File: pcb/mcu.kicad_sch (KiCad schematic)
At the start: 28 parts, among them J1 CON_SAMTEC_14P_2R_1m27_P_KEY_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, U3 IC_MCU_STM32F100C4T6B_48LQFP, X1 XTAL_8M_20PPM_18pF_ECS-80-18-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, X2 XTAL_32K768_10PPM_7pF_ECS-.32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

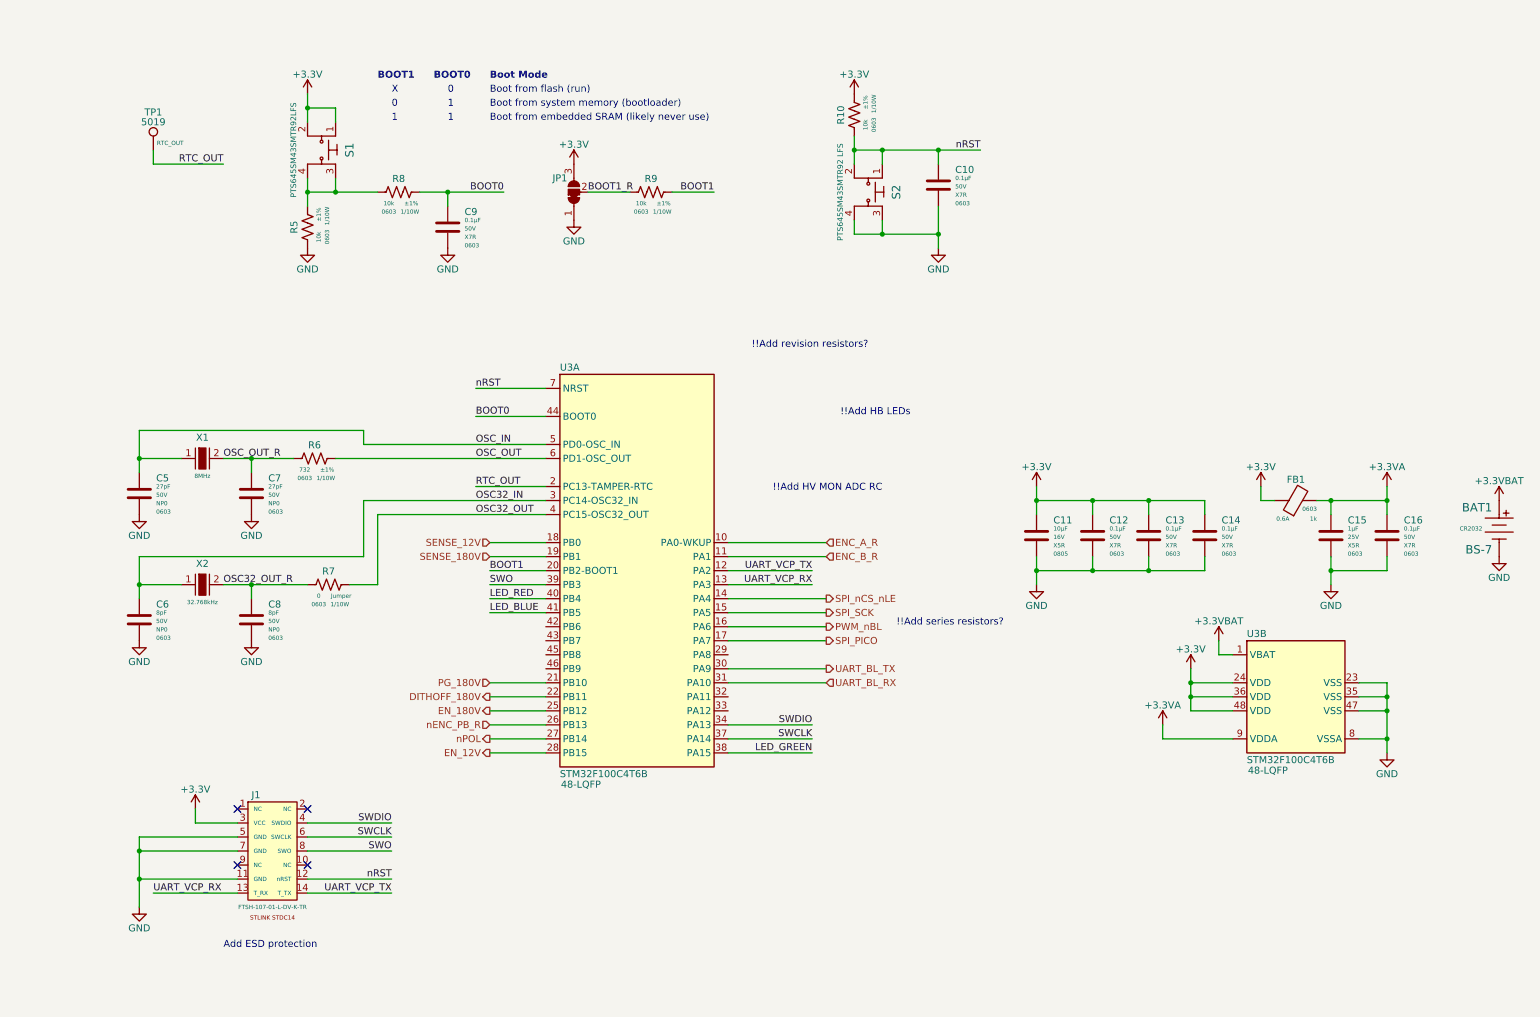
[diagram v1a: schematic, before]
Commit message: Added ESD protection to 5V input, leds, hw rev pins, and test points.
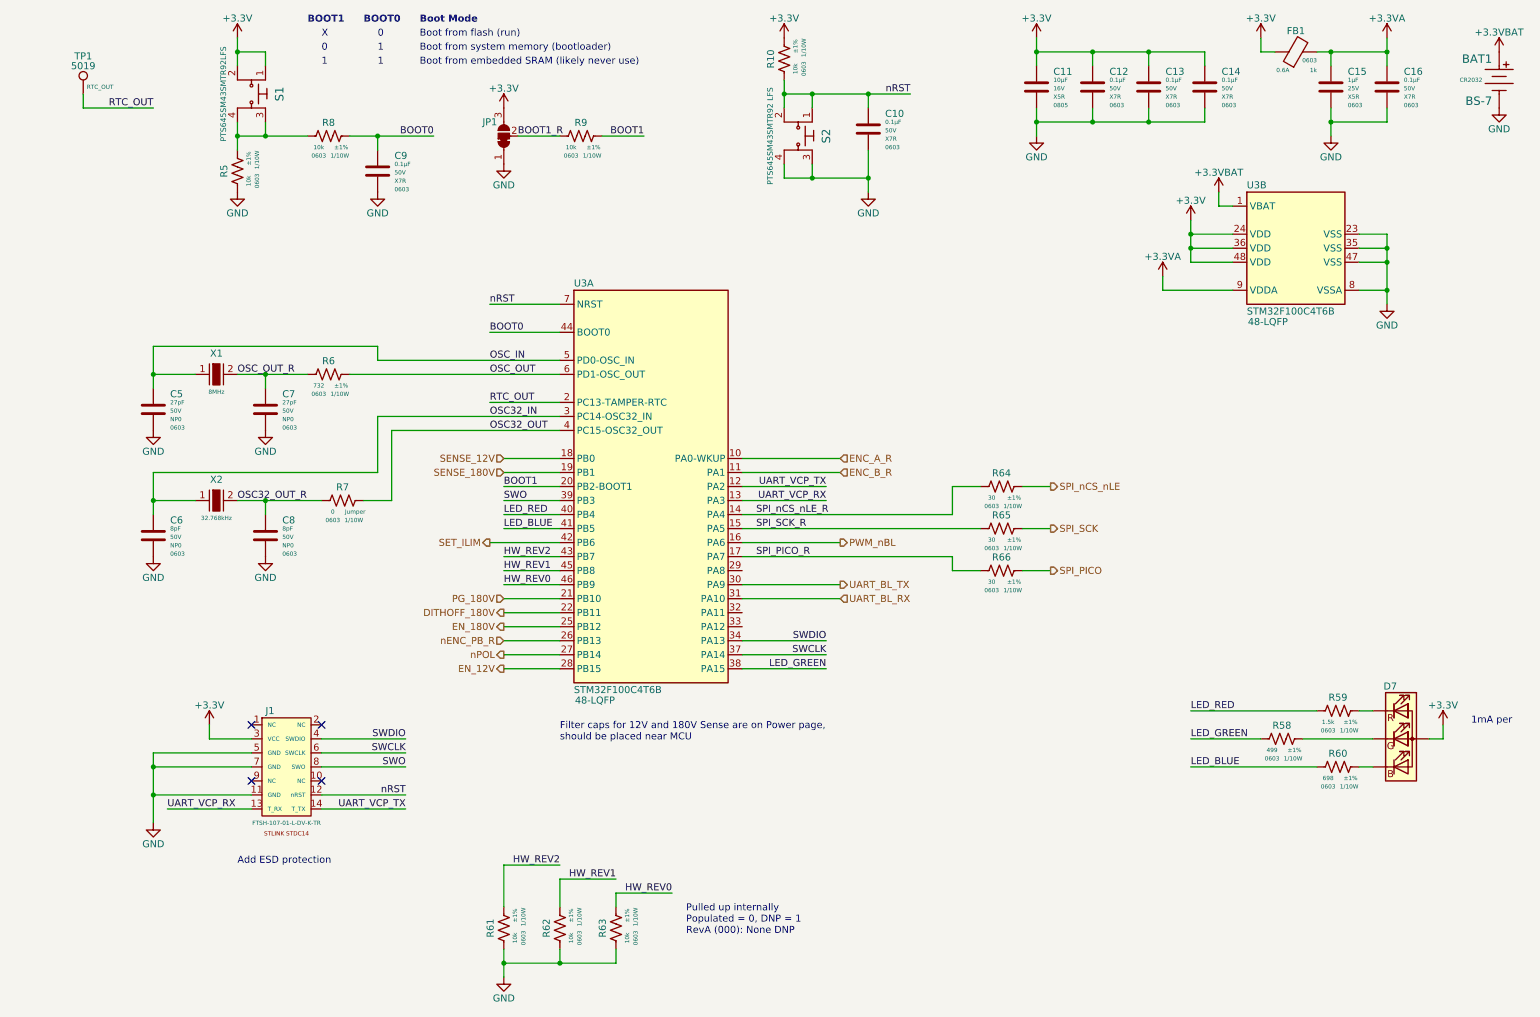
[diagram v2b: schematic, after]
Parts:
- added D7: LED_RGB_0606, arjun_footprints:EAST1616RGBB2_EVE, symbol .arjun:LED_RGB_0606
- added R58: RES_499R_1P_1/10W_0603, Resistor_SMD:R_0603_1608Metric, symbol .arjun:RES_499R_1P_1/10W_0603
- added R59: RES_1K5_1P_1/10W_0603, Resistor_SMD:R_0603_1608Metric, symbol .arjun:RES_1K5_1P_1/10W_0603
- added R60: RES_698R_1P_1/10W_0603, Resistor_SMD:R_0603_1608Metric, symbol .arjun:RES_698R_1P_1/10W_0603
- added R61, R62, R63: RES_10K_1P_1/10W_0603, Resistor_SMD:R_0603_1608Metric, symbol .arjun:RES_10K_1P_1/10W_0603
- added R64, R65, R66: RES_30R_1P_1/10W_0603, Resistor_SMD:R_0603_1608Metric, symbol .arjun:RES_30R_1P_1/10W_0603
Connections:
- net +3.3V: now also D7.4 (A)
- net GND: now also R61.2, R62.2, R63.2
- net LED_BLUE: now also R60.2
- net LED_GREEN: now also R58.2
- net LED_RED: now also R59.2
- net SPI_PICO: now also R66.1; no longer U3.17 (PA7)
- net SPI_SCK: now also R65.1; no longer U3.15 (PA5)
- net SPI_nCS_nLE: now also R64.1; no longer U3.14 (PA4)
- net SET_ILIM: now reaches U3.42 (PB6)
- net HW_REV2: now reaches U3.43 (PB7)
- net HW_REV2: now also R61.1
- net HW_REV1: now reaches U3.45 (PB8)
- net HW_REV1: now also R62.1
- net HW_REV0: now reaches U3.46 (PB9)
- net HW_REV0: now also R63.1
- new net: D7.2 (GK), R58.1
- new net: D7.3 (BK), R60.1
- new net: D7.1 (RK), R59.1
- new net SPI_PICO_R: R66.2, U3.17 (PA7)
- new net SPI_SCK_R: R65.2, U3.15 (PA5)
- new net SPI_nCS_nLE_R: R64.2, U3.14 (PA4)
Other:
- note added: "1mA per"
- note added: "Filter caps for 12V and 180V Sense are on Power page, should be placed near MCU"
- note added: "Pulled up internally Populated = 0, DNP = 1 RevA (000): None DNP"
- note removed: "!!Add HB LEDs"
- note removed: "!!Add HV MON ADC RC"
- note removed: "!!Add revision resistors?"
- note removed: "!!Add series resistors?"
- moved on the sheet: BAT1, C10, C11, C12, C13, C14, C15, C16, C5, C6, C7, C8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

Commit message: Fixed a bunch of footprints and added missing 3D models
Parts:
- removed X1: XTAL_8M_20PPM_18pF_ECS-80-18-30-JGN-TR, arjun_footprints:SMD-2_5x3.2mm_ECS, symbol arjun_symbols:XTAL_8M_20PPM_18pF_ECS-80-18-30-JGN-TR
- removed X2: XTAL_32K768_10PPM_7pF_ECS-.327-7-34B-C-TR, arjun_footprints:SMD-2_3.2x1.5mm_ECS, symbol arjun_symbols:XTAL_32K768_10PPM_7pF_ECS-.327-7-34B-C-TR
- added X1: XTAL_8M_20PPM_18pF_ECS-80-18-30-JGN-TR, arjun_footprints:SMD-2_5x3.2mm_ECS, symbol .arjun:XTAL_8M_20PPM_18pF_ECS-80-18-30-JGN-TR
- added X2: XTAL_32K768_10PPM_7pF_ECS-.327-7-34B-C-TR, arjun_footprints:SMD-2_3.2x1.5mm_ECS, symbol .arjun:XTAL_32K768_10PPM_7pF_ECS-.327-7-34B-C-TR
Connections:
- net OSC32_IN: now also X2.1
- net OSC32_OUT_R: now also X2.2
- net OSC_IN: now also X1.1
- net OSC_OUT_R: now also X1.2

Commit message: Started layout!! 180V boost mostly laid out
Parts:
- R10, R5, R8, R9: symbol arjun_symbols:RES_10K_1P_1/10W_0603 -> arjun_symbols:RES_10K_1P_1/10W_0603
- R58: symbol .arjun:RES_499R_1P_1/10W_0603 -> .arjun:RES_499R_1P_1/10W_0603
- R59: symbol .arjun:RES_1K5_1P_1/10W_0603 -> .arjun:RES_1K5_1P_1/10W_0603
- R6: symbol arjun_symbols:RES_732R_1P_1/10W_0603 -> arjun_symbols:RES_732R_1P_1/10W_0603
- R60: symbol .arjun:RES_698R_1P_1/10W_0603 -> .arjun:RES_698R_1P_1/10W_0603
- R61, R62, R63: symbol .arjun:RES_10K_1P_1/10W_0603 -> .arjun:RES_10K_1P_1/10W_0603
- R64, R65, R66: symbol .arjun:RES_30R_1P_1/10W_0603 -> .arjun:RES_30R_1P_1/10W_0603
- R7: symbol arjun_symbols:RES_0R_1/10W_0603 -> arjun_symbols:RES_0R_1/10W_0603
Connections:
- net 180V renamed +3.3VBAT
- no-connect marks 4 -> 7

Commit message: Started mcu placement
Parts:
- added C43: CAP_CER_0u1_50V_X7R_0603, Capacitor_SMD:C_0603_1608Metric, symbol arjun_symbols:CAP_CER_0u1_50V_X7R_0603
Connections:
- net +3.3VBAT: now also C43.1
- net GND: now also C43.2
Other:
- moved on the sheet: BAT1, C10, C11, C12, C13, C14, C15, C16, FB1, R10, S2

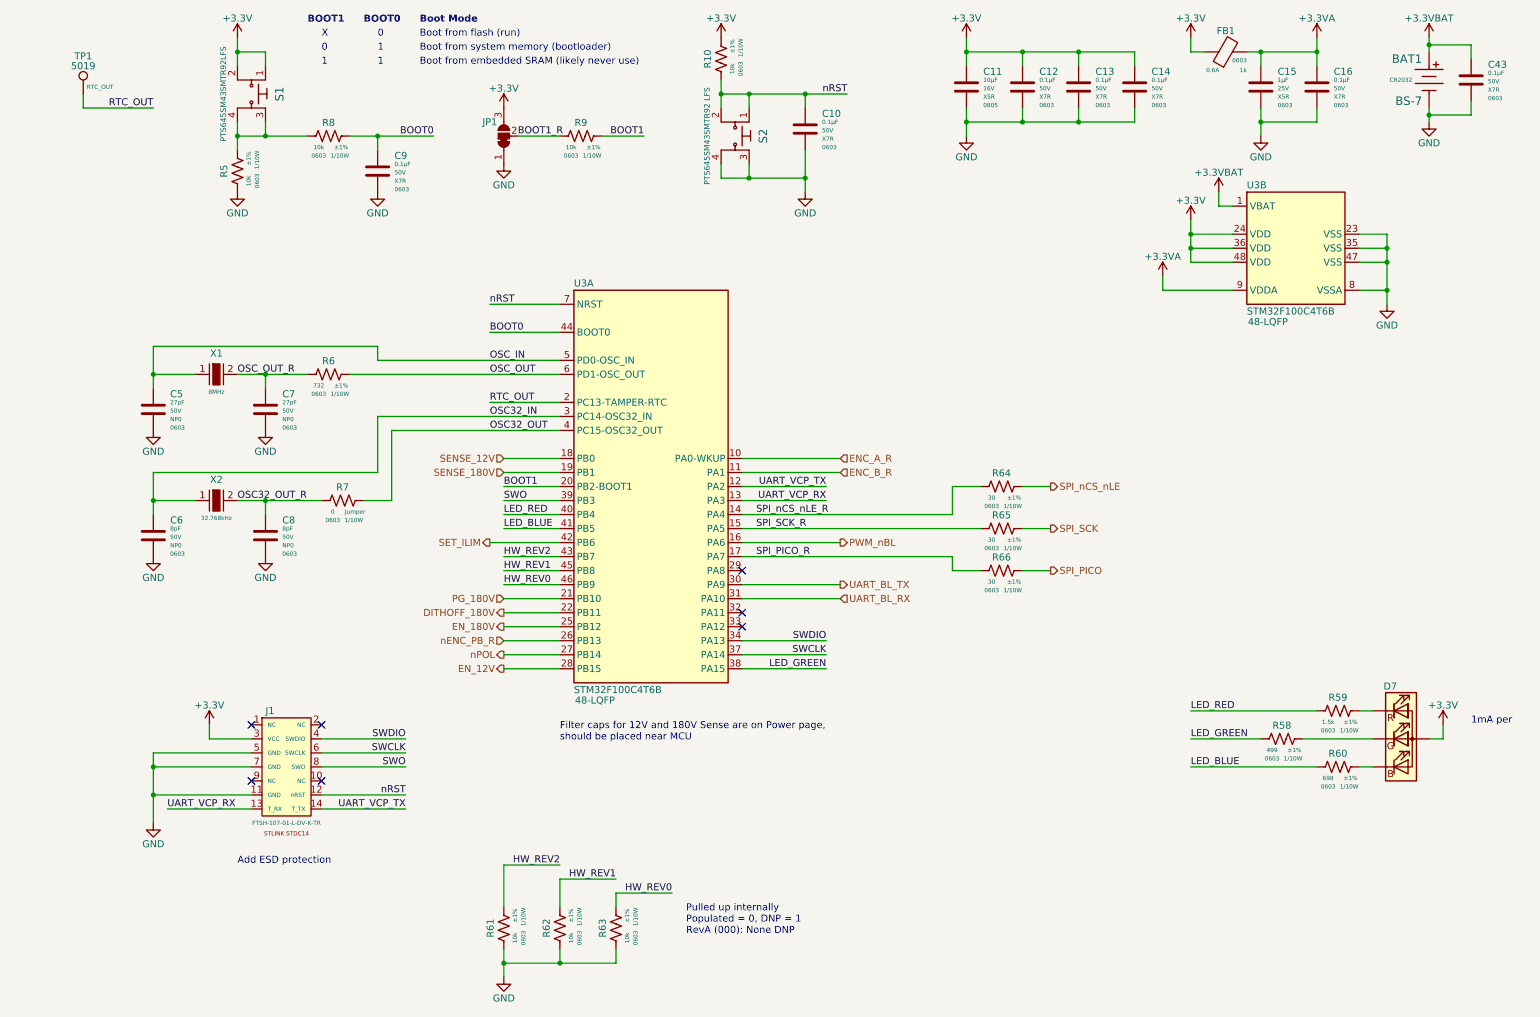
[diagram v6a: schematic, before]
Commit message: Placement V1. Want to try and centre the board on the nixies vertically. Saving progress before trying out different placements.
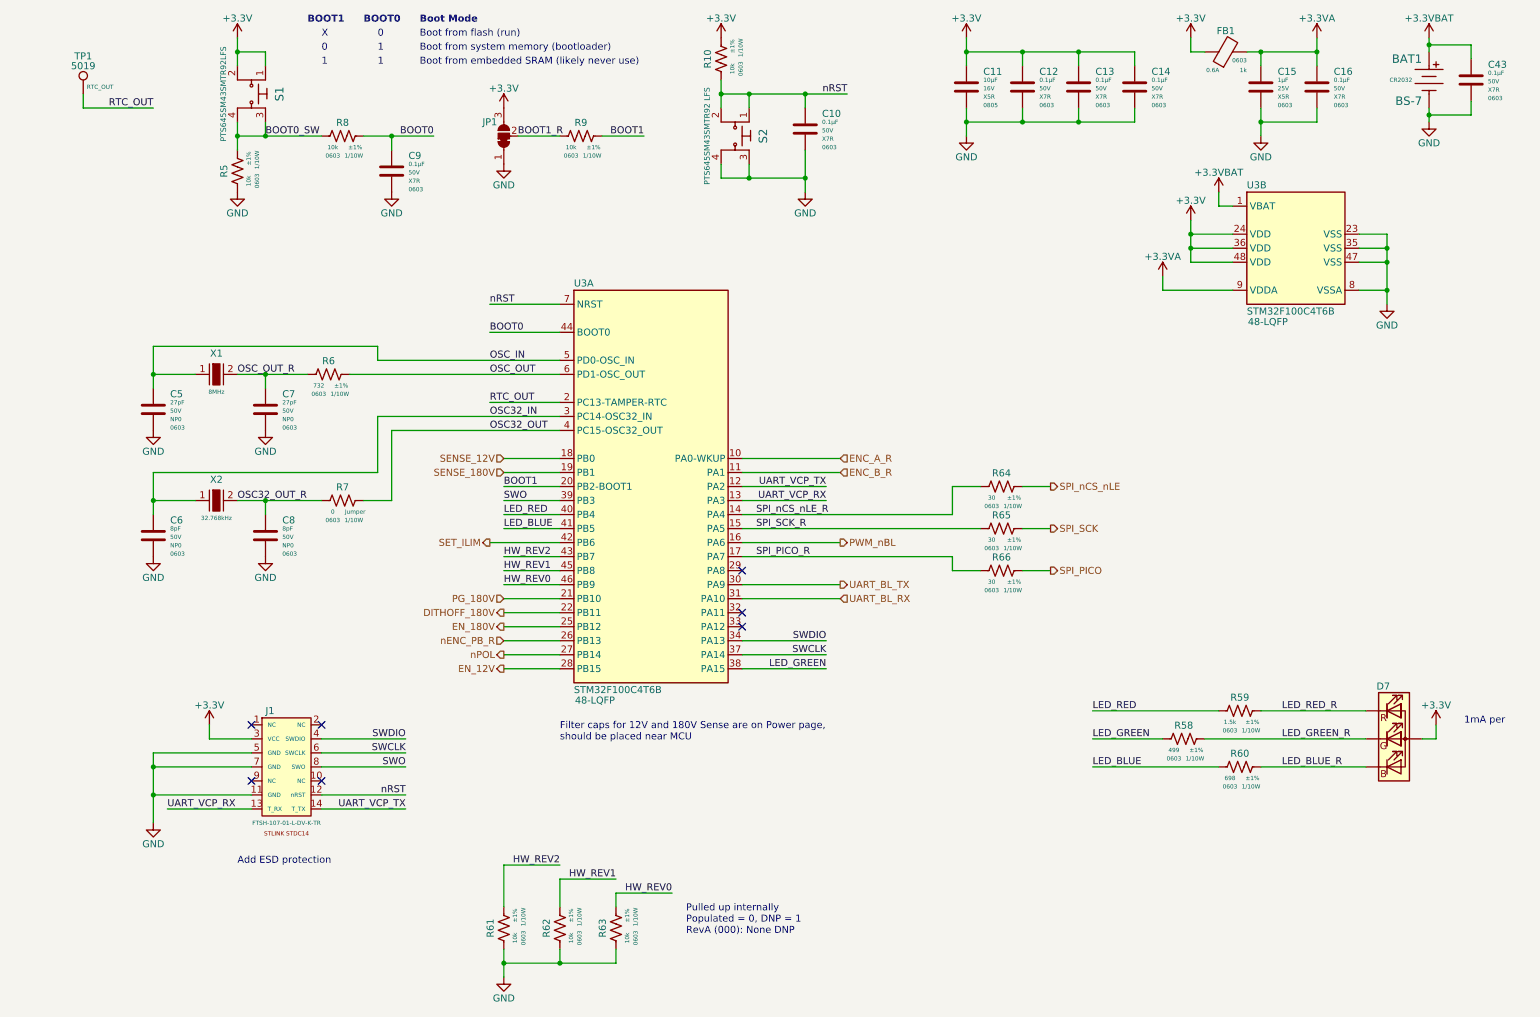
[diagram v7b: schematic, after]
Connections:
- net LED_GREEN_R: now reaches D7.2 (GK), R58.1
- net BOOT0_SW: now reaches R5.1, R8.2, S1.3, S1.4
- net LED_BLUE_R: now reaches D7.3 (BK), R60.1
- net LED_RED_R: now reaches D7.1 (RK), R59.1
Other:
- moved on the sheet: C9, D7, R58, R59, R60, R8

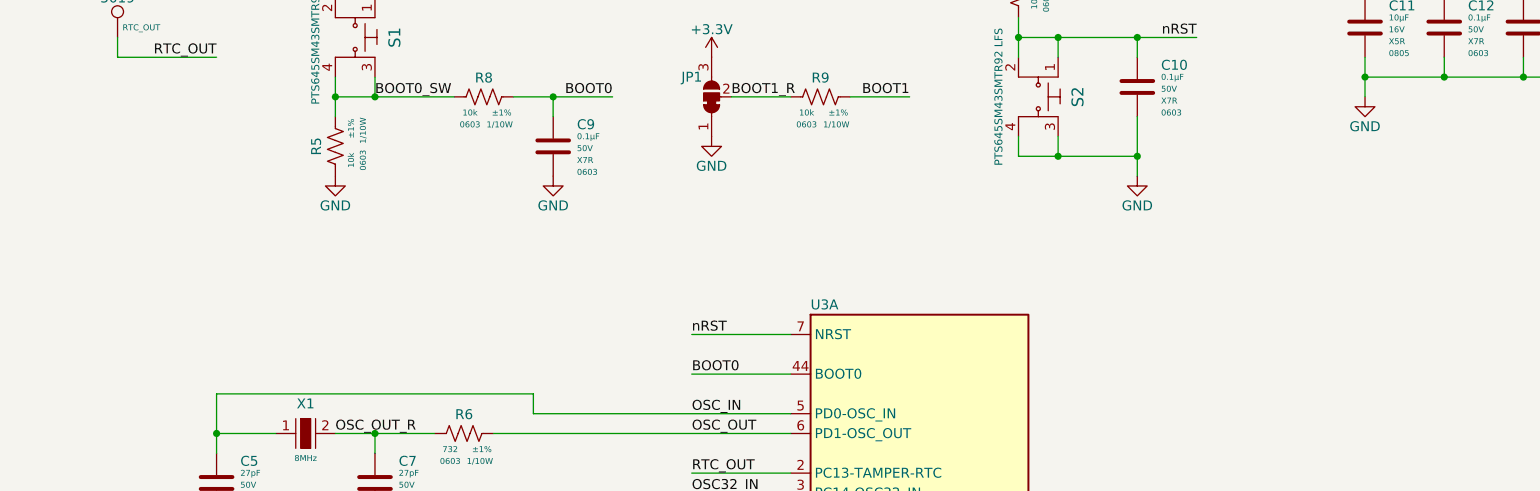
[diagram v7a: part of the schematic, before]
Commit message: Added note about mcu reset
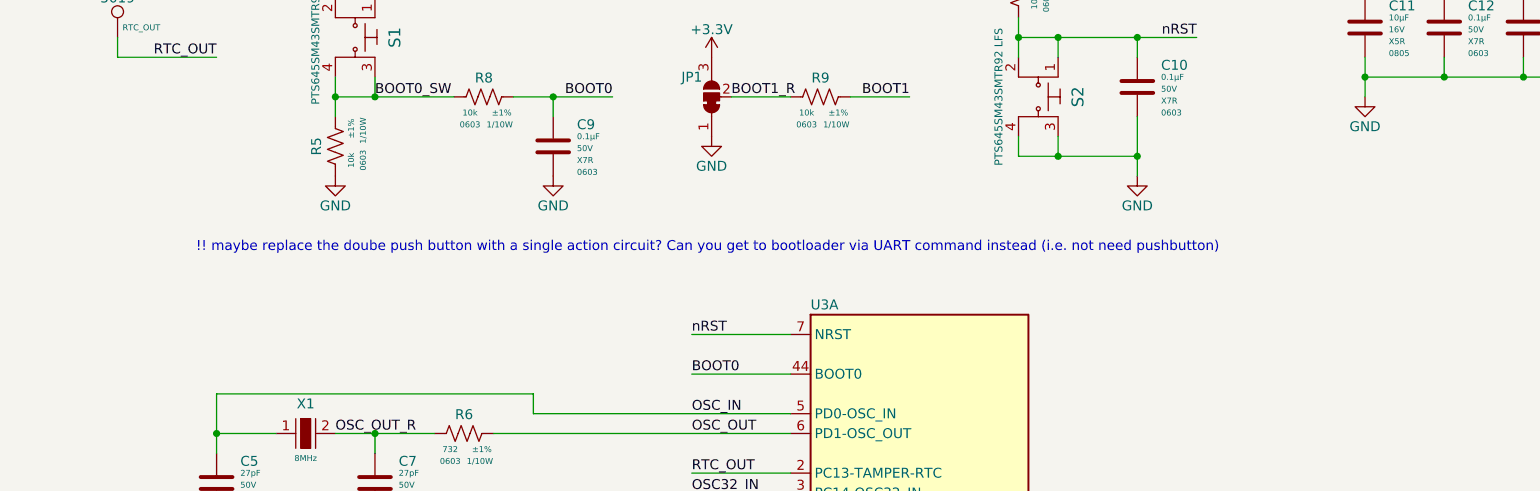
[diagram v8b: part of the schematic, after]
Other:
- note added: "!! maybe replace the doube push button with a single action circuit? Can you get to bootloader via UART command instead (i.e. not need pushbutton)"
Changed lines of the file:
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@@
+		)
+	)
+	(text "!! maybe replace the doube push button with a single action circuit? Can you get to bootloader via UART command instead (i.e. not need pushbutton)"
+		(exclude_from_sim no)
+		(at 93.472 57.404 0)
+		(effects
+			(font
+				(size 1.27 1.27)
+			)
 		)
 	)
